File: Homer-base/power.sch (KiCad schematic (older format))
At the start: 6 parts

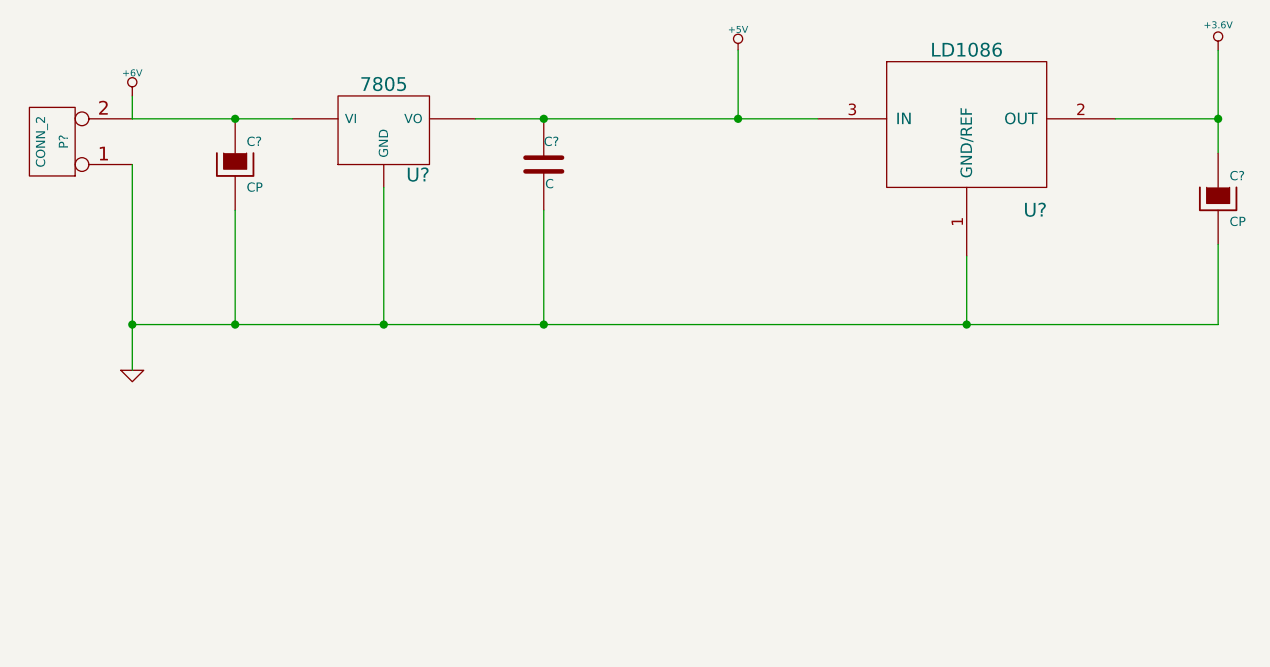
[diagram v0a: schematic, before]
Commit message: Add varistor and AC/DC
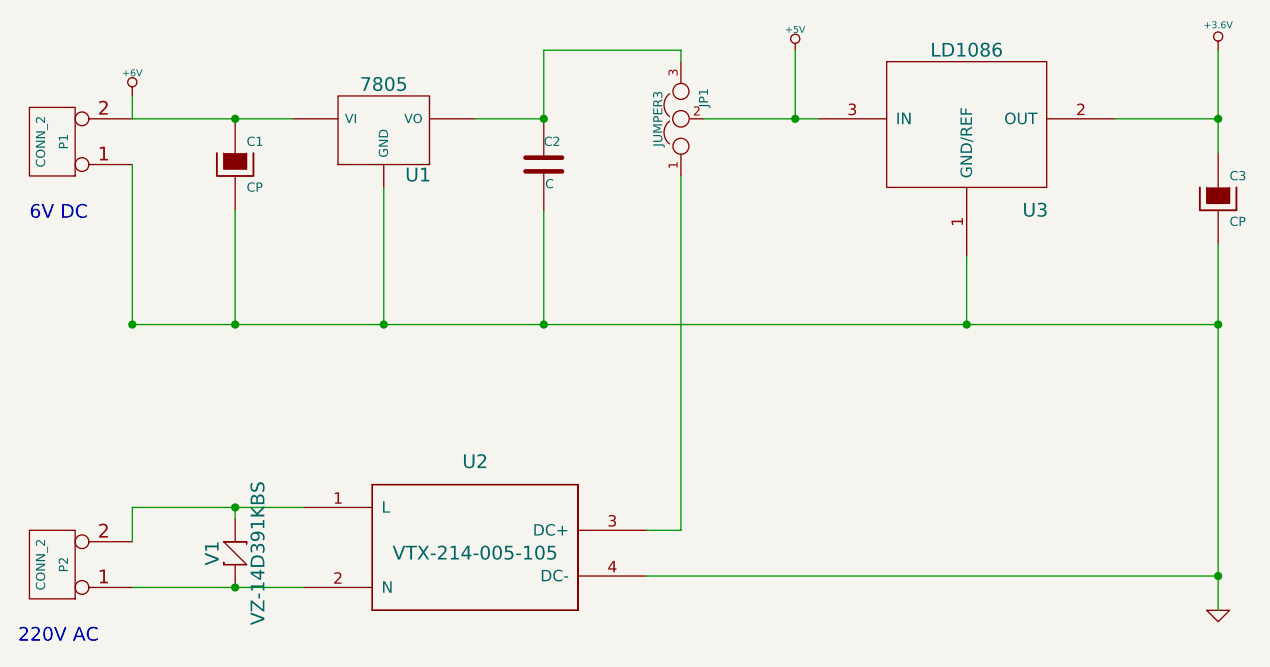
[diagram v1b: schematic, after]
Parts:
- added JP1: JUMPER3, ~, symbol JUMPER3
- added P2: CONN_2, symbol CONN_2
- added U2: VTX-214-005-105, symbol VTX-214-005-105
- added V1: VZ-14D391KBS, symbol VZ-14D391KBS
- gave numbers to parts that had none: 6
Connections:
- net +5V: now also JP1.2; no longer C2.1, U1.VO
- net GND: now also U2.4 (DC-)
- new net: C2.1, JP1.3, U1.VO
- new net: P2.1 (P1), U2.2 (N), V1.2
- new net: P2.2 (PM), U2.1 (L), V1.1
- new net: JP1.1, U2.3 (DC+)
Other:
- note added: "220V AC"
- note added: "6V DC"
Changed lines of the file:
@@
 LIBS:valves
 LIBS:MyKicadLib
+LIBS:varistor
 LIBS:power-cache
 EELAYER 27 0
@@
 Sheet 1 1
 Title "noname.sch"
-Date "1 jan 2016"
+Date "11 feb 2017"
 Rev ""
 Comp ""
@@
 $EndDescr
 $Comp
-L CONN_2 P?
+L CONN_2 P1
 U 1 1 5664998F
 P 1050 1550
-F 0 "P?" V 1000 1550 40  0000 C CNN
+F 0 "P1" V 1000 1550 40  0000 C CNN
 F 1 "CONN_2" V 1100 1550 40  0000 C CNN
 F 2 "" H 1050 1550 60  0000 C CNN
@@
 $EndComp
 $Comp
-L 7805 U?
+L 7805 U1
 U 1 1 566499CF
 P 2500 1500
-F 0 "U?" H 2650 1304 60  0000 C CNN
+F 0 "U1" H 2650 1304 60  0000 C CNN
 F 1 "7805" H 2500 1700 60  0000 C CNN
 F 2 "" H 2500 1500 60  0000 C CNN
@@
 $EndComp
 $Comp
-L C C?
+L C C2
 U 1 1 56649A12
 P 3200 1650
-F 0 "C?" H 3200 1750 40  0000 L CNN
+F 0 "C2" H 3200 1750 40  0000 L CNN
 F 1 "C" H 3206 1565 40  0000 L CNN
 F 2 "~" H 3238 1500 30  0000 C CNN
@@
 $EndComp
 $Comp
-L CP C?
+L CP C1
 U 1 1 56649A21
 P 1850 1650
-F 0 "C?" H 1900 1750 40  0000 L CNN
+F 0 "C1" H 1900 1750 40  0000 L CNN
 F 1 "CP" H 1900 1550 40  0000 L CNN
 F 2 "~" H 1950 1500 30  0000 C CNN
@@
 Connection ~ 1850 1450
 Wire Wire Line
-	1400 1650 1400 2550
-Wire Wire Line
 	1400 2350 6150 2350
 Wire Wire Line
@@
 Connection ~ 1850 2350
 Wire Wire Line
-	2900 1450 4400 1450
+	2900 1450 3200 1450
+Wire Wire Line
+	3900 1450 4400 1450
 Wire Wire Line
 	1400 1350 1400 1450
 $Comp
-L GND #PWR?
+L GND #PWR4
 U 1 1 56649B65
-P 1400 2550
-F 0 "#PWR?" H 1400 2550 30  0001 C CNN
-F 1 "GND" H 1400 2480 30  0001 C CNN
-F 2 "" H 1400 2550 60  0000 C CNN
-F 3 "" H 1400 2550 60  0000 C CNN
-	1    1400 2550
-	1    0    0    -1
-$EndComp
-$Comp
-L +6V #PWR?
+P 6150 3600
+F 0 "#PWR4" H 6150 3600 30  0001 C CNN
+F 1 "GND" H 6150 3530 30  0001 C CNN
+F 2 "" H 6150 3600 60  0000 C CNN
+F 3 "" H 6150 3600 60  0000 C CNN
+	1    6150 3600
+	1    0    0    -1
+$EndComp
+$Comp
+L +6V #PWR1
 U 1 1 56649B8F
 P 1400 1350
-F 0 "#PWR?" H 1400 1480 20  0001 C CNN
+F 0 "#PWR1" H 1400 1480 20  0001 C CNN
 F 1 "+6V" H 1400 1450 30  0000 C CNN
 F 2 "" H 1400 1350 60  0000 C CNN
@@
 Connection ~ 1400 2350
 $Comp
-L LD1086 U?
+L LD1086 U3
 U 1 1 56649F4E
 P 5100 1150
-F 0 "U?" H 5350 450 60  0000 C CNN
+F 0 "U3" H 5350 450 60  0000 C CNN
 F 1 "LD1086" H 5050 1150 60  0000 C CNN
 F 2 "" H 5100 1350 60  0000 C CNN
@@
 Connection ~ 5050 2350
 $Comp
-L CP C?
+L CP C3
 U 1 1 56869925
 P 6150 1800
-F 0 "C?" H 6200 1900 40  0000 L CNN
+F 0 "C3" H 6200 1900 40  0000 L CNN
 F 1 "CP" H 6200 1700 40  0000 L CNN
 F 2 "~" H 6250 1650 30  0000 C CNN
@@
 	6150 1150 6150 1600
 Wire Wire Line
-	6150 2350 6150 2000
-$Comp
-L +3.6V #PWR?
+	6150 2000 6150 3600
+$Comp
+L +3.6V #PWR3
 U 1 1 5686996D
 P 6150 1150
-F 0 "#PWR?" H 6150 1110 30  0001 C CNN
+F 0 "#PWR3" H 6150 1110 30  0001 C CNN
 F 1 "+3.6V" H 6150 1260 30  0000 C CNN
 F 2 "~" H 6150 1150 60  0000 C CNN
@@
 Connection ~ 6150 1450
 $Comp
-L +5V #PWR?
+L +5V #PWR2
 U 1 1 5686998F
-P 4050 1150
-F 0 "#PWR?" H 4050 1240 20  0001 C CNN
-F 1 "+5V" H 4050 1240 30  0000 C CNN
-F 2 "" H 4050 1150 60  0000 C CNN
-F 3 "" H 4050 1150 60  0000 C CNN
-	1    4050 1150
-	1    0    0    -1
-$EndComp
-Wire Wire Line
-	4050 1150 4050 1450
-Connection ~ 4050 1450
+P 4300 1150
+F 0 "#PWR2" H 4300 1240 20  0001 C CNN
+F 1 "+5V" H 4300 1240 30  0000 C CNN
+F 2 "" H 4300 1150 60  0000 C CNN
+F 3 "" H 4300 1150 60  0000 C CNN
+	1    4300 1150
+	1    0    0    -1
+$EndComp
+Wire Wire Line
+	4300 1150 4300 1450
+Connection ~ 4300 1450
+$Comp
+L CONN_2 P2
+U 1 1 589EC88C
+P 1050 3400
+F 0 "P2" V 1000 3400 40  0000 C CNN
+F 1 "CONN_2" V 1100 3400 40  0000 C CNN
+F 2 "" H 1050 3400 60  0000 C CNN
+F 3 "" H 1050 3400 60  0000 C CNN
+	1    1050 3400
+	-1   0    0    1
+$EndComp
+$Comp
+L VTX-214-005-105 U2
+U 1 1 589ECC54
+P 2900 3350
+F 0 "U2" H 2900 3750 60  0000 C CNN
+F 1 "VTX-214-005-105" H 2900 3350 60  0000 C CNN
+F 2 "" H 2900 3350 60  0000 C CNN
+F 3 "" H 2900 3350 60  0000 C CNN
+	1    2900 3350
+	1    0    0    -1
+$EndComp
+$Comp
+L VZ-14D391KBS V1
+U 1 1 589ED8A9
+P 1850 3350
+F 0 "V1" V 1750 3350 60  0000 C CNN
+F 1 "VZ-14D391KBS" V 1950 3350 60  0000 C CNN
+F 2 "" H 1850 3350 60  0000 C CNN
+F 3 "" H 1850 3350 60  0000 C CNN
+	1    1850 3350
+	1    0    0    -1
+$EndComp
+Wire Wire Line
+	1400 3500 2150 3500
+Connection ~ 1850 3500
+Wire Wire Line
+	1400 3150 2150 3150
+Wire Wire Line
+	1400 3150 1400 3300
+Wire Wire Line
+	1850 3200 1850 3150
+Connection ~ 1850 3150
+$Comp
+L JUMPER3 JP1
+U 1 1 589EDAE9
+P 3800 1450
+F 0 "JP1" H 3850 1350 40  0000 L CNN
+F 1 "JUMPER3" H 3800 1550 40  0000 C CNN
+F 2 "~" H 3800 1450 60  0000 C CNN
+F 3 "~" H 3800 1450 60  0000 C CNN
+	1    3800 1450
+	0    -1   -1   0
+$EndComp
+Wire Wire Line
+	3800 1200 3800 1150
+Wire Wire Line
+	3800 1150 3200 1150
+Wire Wire Line
+	3200 1150 3200 1450
+Wire Wire Line
+	3800 1700 3800 3250
+Wire Wire Line
+	3800 3250 3650 3250
+Wire Wire Line
+	6150 3450 3650 3450
+Connection ~ 6150 2350
+Connection ~ 6150 3450
+Wire Wire Line
+	1400 2350 1400 1650
+Text Notes 950  1900 0    60   ~ 0
+6V DC
+Text Notes 900  3750 0    60   ~ 0
+220V AC
 $EndSCHEMATC
